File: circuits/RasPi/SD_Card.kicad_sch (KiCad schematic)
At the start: 6 parts, among them J11 Micro_SD_Card_Det_Hirose_DM3AT, Q27 BSS138, Q28 SSM3J332R

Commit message: 更新
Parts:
- removed Q27: BSS138, Package_TO_SOT_SMD:SOT-23, symbol Device:Q_NMOS_GSD
- added Q27: 2N7002, Package_TO_SOT_SMD:SOT-23, symbol Transistor_FET:2N7002
- J11: footprint (none) -> TomoshibiLibrary:Connector_SDCard_DM3AT
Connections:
- net GNDD: now also J11.MP (SHIELD), Q27.2 (S); no longer J11.11 (SHIELD)
- net PWR_ON: now also Q27.1 (G)
- net at Q28.1 (G), R104.1: now also Q27.3 (D)
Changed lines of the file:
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@@
       (effects (font (size 1.27 1.27)))
     )
-    (property "Footprint" "" (at 209.55 53.34 0)
+    (property "Footprint" "TomoshibiLibrary:Connector_SDCard_DM3AT" (at 209.55 53.34 0)
       (effects (font (size 1.27 1.27)) hide)
     )
@@
     )
     (pin "8")
-    (pin "10")
+    (pin "A")
     (pin "3")
     (pin "2")
     (pin "6")
     (pin "5")
-    (pin "11")
+    (pin "B")
     (pin "1")
     (pin "4")
     (pin "7")
-    (pin "9")
+    (pin "MP")
     (instances
       (project "RasPi"
@@
     )
   )
+  (symbol (lib_id "Transistor_FET:2N7002") (at 147.32 129.54 0) (unit 1)
+    (in_bom yes) (on_board yes) (dnp no)
+    (property "Reference" "Q27" (at 152.4 129.54 0)
+      (effects (font (size 1.27 1.27)) (justify left))
+    )
+    (property "Value" "2N7002" (at 152.4 132.08 0)
+      (effects (font (size 1.27 1.27)) (justify left))
+    )
+    (property "Footprint" "Package_TO_SOT_SMD:SOT-23" (at 152.4 131.445 0)
+      (effects (font (size 1.27 1.27) italic) (justify left) hide)
+    )
+    (property "Datasheet" "https://www.onsemi.com/pub/Collateral/NDS7002A-D.PDF" (at 152.4 133.35 0)
+      (effects (font (size 1.27 1.27)) (justify left) hide)
+    )
+    (pin "3")
+    (pin "1")
+    (pin "2")
+    (instances
+      (project "RasPi"
+        (path "/689a9e74-f202-4ea4-bfbb-4341f2549250/fddad0c3-2af8-46e3-8794-fa1122d24d51/2ec7d498-8e54-4c52-b9ab-4312d8412cc4"
+          (reference "Q27") (unit 1)
+        )
+      )
+    )
+  )
   (symbol (lib_id "power:GNDD") (at 114.3 78.74 0) (unit 1)
     (in_bom yes) (on_board yes) (dnp no)
@@
         )
       )
-    )
-  )
-  (symbol (lib_name "Q_NMOS_GSD_1") (lib_id "Device:Q_NMOS_GSD") (at 147.32 129.54 0) (unit 1)
-    (in_bom yes) (on_board yes) (dnp no)
-    (property "Reference" "Q27" (at 152.4 129.54 0)
-      (effects (font (size 1.27 1.27)) (justify left))
-    )
-    (property "Value" "BSS138" (at 152.4 132.08 0)
-      (effects (font (size 1.27 1.27)) (justify left))
-    )
-    (property "Footprint" "Package_TO_SOT_SMD:SOT-23" (at 152.4 127 0)
-      (effects (font (size 1.27 1.27)) hide)
-    )
-    (property "Datasheet" "~" (at 147.32 129.54 0)
-      (effects (font (size 1.27 1.27)) hide)
-    )
-    (pin "1")
-    (pin "2")
-    (pin "3")
-    (instances
-      (project "RasPi"
-        (path "/689a9e74-f202-4ea4-bfbb-4341f2549250/fddad0c3-2af8-46e3-8794-fa1122d24d51/2ec7d498-8e54-4c52-b9ab-4312d8412cc4"
-          (reference "Q27") (unit 1)
-        )
-      )

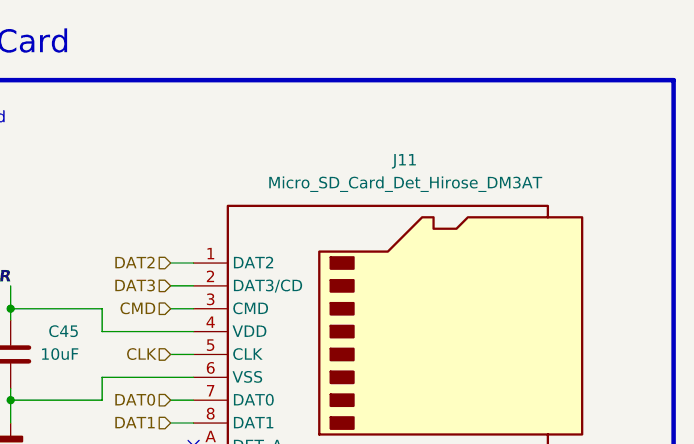
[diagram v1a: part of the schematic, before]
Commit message: 発注第2弾
RasPi発注
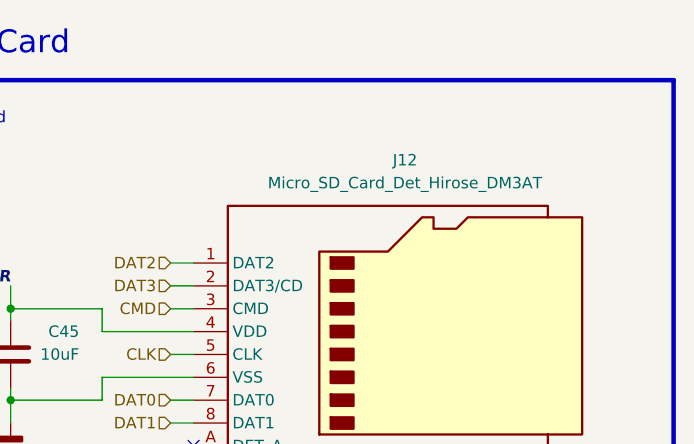
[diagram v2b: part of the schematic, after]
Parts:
- Q27: footprint Package_TO_SOT_SMD:SOT-23 -> Package_TO_SOT_SMD:SC-59
- renumbered J11 to J12
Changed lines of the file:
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@@
   (symbol (lib_id "Connector:Micro_SD_Card_Det_Hirose_DM3AT") (at 157.48 71.12 0) (unit 1)
     (in_bom yes) (on_board yes) (dnp no) (fields_autoplaced)
-    (property "Reference" "J11" (at 158.115 49.53 0)
+    (property "Reference" "J12" (at 158.115 49.53 0)
       (effects (font (size 1.27 1.27)))
     )
@@
       (project "RasPi"
         (path "/689a9e74-f202-4ea4-bfbb-4341f2549250/fddad0c3-2af8-46e3-8794-fa1122d24d51/2ec7d498-8e54-4c52-b9ab-4312d8412cc4"
-          (reference "J11") (unit 1)
+          (reference "J12") (unit 1)
         )
       )
@@
       (effects (font (size 1.27 1.27)) (justify left))
     )
-    (property "Footprint" "Package_TO_SOT_SMD:SOT-23" (at 152.4 131.445 0)
+    (property "Footprint" "Package_TO_SOT_SMD:SC-59" (at 152.4 131.445 0)
       (effects (font (size 1.27 1.27) italic) (justify left) hide)
     )
